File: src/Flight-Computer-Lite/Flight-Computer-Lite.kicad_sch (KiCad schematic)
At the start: 38 parts, among them J1 Jumper_NO, J2 Jumper_NO, P1 1546551-2, P2 3220-20-0200-00, U1 STM32H750VBTx, U2 LMS8117AMP-3.3_NOPB, Y1 ECS-240-18-33-JGN-TR

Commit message: imported footprints into layout
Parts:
- B1: footprint SW_PTS647SM38SMTR2LFS_CNK -> Flight-Computer-Lite:PTS647SM38SMTR2LFS
- C1, C11, C12, C14, C15, C2, C3, C4, C5, C6, C7, C8, C9: footprint Flight-Computer:CAP_0603 -> Flight-Computer-Lite:CAP_0603
- C10, C13: footprint Flight-Computer:T491A106K010AT -> Flight-Computer-Lite:T491A106K010AT
- D1: footprint LED_CLMVC-FKA-CL1D1L71BB7C3C3 -> Flight-Computer-Lite:CLMVC-FKA-CL1D1L71BB7C3C3
- D2, D3: footprint SOD-123FL_MCC -> Flight-Computer-Lite:SM5819PL-TP
- H1, H2, H3: footprint Flight-Computer:MountingHole_3mm -> Flight-Computer-Lite:MountingHole_3mm
- J1, J2: footprint Engine-Controller:Jumper-NO -> Flight-Computer-Lite:Jumper-NO
- LOGO1: footprint Flight-Computer:Logo -> Flight-Computer-Lite:Logo
- P1: footprint Flight-Computer:1546551-2 -> Flight-Computer-Lite:1546551-2
- P2: footprint CONN20_D10-RA-BK_SUL -> Flight-Computer-Lite:3220-20-0200-00
- R1, R2, R3, R4, R5, R6: footprint Flight-Computer:RES_0603 -> Flight-Computer-Lite:RES_0603
- TP1: footprint Flight-Computer:TP -> Flight-Computer-Lite:TP
- U2: footprint Flight-Computer:LMS8117AMP-3.3NOPB -> Flight-Computer-Lite:LMS8117AMP-3.3NOPB
- Y1: footprint Flight-Computer:ECS-240-18-33-JGN-TR -> Flight-Computer-Lite:ECS-240-18-33-JGN-TR

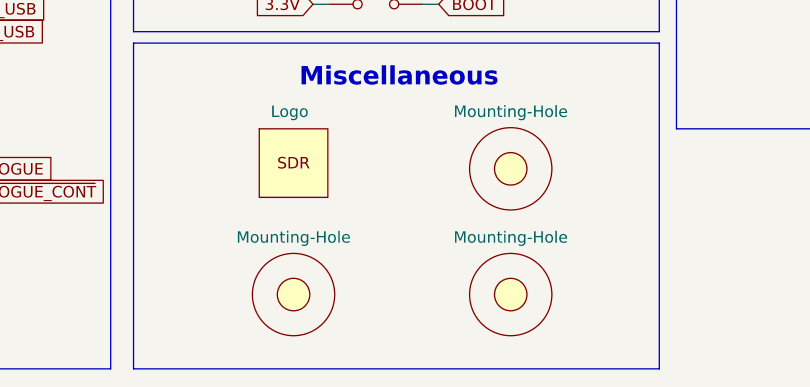
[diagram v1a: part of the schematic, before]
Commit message: finalized board outline and component placements
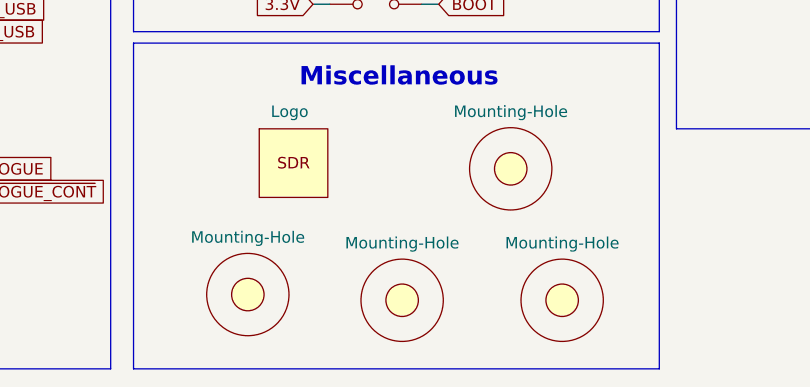
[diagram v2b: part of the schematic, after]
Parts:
- added H4: Mounting-Hole, Flight-Computer-Lite:MountingHole_3mm, symbol Flight-Computer-Lite:Mounting-Hole
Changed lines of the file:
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@@
     (pin "2")
   )
-  (symbol (lib_id "Flight-Computer:Mounting-Hole") (at 135.255 182.88 0) (unit 1)
-    (in_bom yes) (on_board yes)
-    (property "Reference" "H1" (id 0) (at 135.255 176.53 0)
-      (effects (font (size 1.27 1.27)) hide)
-    )
-    (property "Value" "Mounting-Hole" (id 1) (at 135.255 176.53 0))
-    (property "Footprint" "Flight-Computer-Lite:MountingHole_3mm" (id 2) (at 135.255 182.88 0)
-      (effects (font (size 1.27 1.27)) hide)
-    )
-    (property "Datasheet" "" (id 3) (at 135.255 182.88 0)
+  (symbol (lib_id "Flight-Computer:Mounting-Hole") (at 130.175 182.88 0) (unit 1)
+    (in_bom yes) (on_board yes)
+    (property "Reference" "H1" (id 0) (at 130.175 176.53 0)
+      (effects (font (size 1.27 1.27)) hide)
+    )
+    (property "Value" "Mounting-Hole" (id 1) (at 130.175 176.53 0))
+    (property "Footprint" "Flight-Computer-Lite:MountingHole_3mm" (id 2) (at 130.175 182.88 0)
+      (effects (font (size 1.27 1.27)) hide)
+    )
+    (property "Datasheet" "" (id 3) (at 130.175 182.88 0)
       (effects (font (size 1.27 1.27)) hide)
     )
@@
     (pin "3")
   )
-  (symbol (lib_id "Flight-Computer:Mounting-Hole") (at 159.385 182.88 0) (unit 1)
-    (in_bom yes) (on_board yes)
-    (property "Reference" "H3" (id 0) (at 159.385 176.53 0)
-      (effects (font (size 1.27 1.27)) hide)
-    )
-    (property "Value" "Mounting-Hole" (id 1) (at 159.385 176.53 0))
-    (property "Footprint" "Flight-Computer-Lite:MountingHole_3mm" (id 2) (at 159.385 182.88 0)
-      (effects (font (size 1.27 1.27)) hide)
-    )
-    (property "Datasheet" "" (id 3) (at 159.385 182.88 0)
+  (symbol (lib_id "Flight-Computer:Mounting-Hole") (at 165.1 183.515 0) (unit 1)
+    (in_bom yes) (on_board yes)
+    (property "Reference" "H3" (id 0) (at 165.1 177.165 0)
+      (effects (font (size 1.27 1.27)) hide)
+    )
+    (property "Value" "Mounting-Hole" (id 1) (at 165.1 177.165 0))
+    (property "Footprint" "Flight-Computer-Lite:MountingHole_3mm" (id 2) (at 165.1 183.515 0)
+      (effects (font (size 1.27 1.27)) hide)
+    )
+    (property "Datasheet" "" (id 3) (at 165.1 183.515 0)
       (effects (font (size 1.27 1.27)) hide)
     )
@@
     (pin "1")
     (pin "2")
+  )
+  (symbol (lib_id "Flight-Computer-Lite:Mounting-Hole") (at 147.32 183.515 0) (unit 1)
+    (in_bom yes) (on_board yes)
+    (property "Reference" "H4" (id 0) (at 147.32 177.165 0)
+      (effects (font (size 1.27 1.27)) hide)
+    )
+    (property "Value" "Mounting-Hole" (id 1) (at 147.32 177.165 0))
+    (property "Footprint" "Flight-Computer-Lite:MountingHole_3mm" (id 2) (at 147.32 183.515 0)
+      (effects (font (size 1.27 1.27)) hide)
+    )
+    (property "Datasheet" "" (id 3) (at 147.32 183.515 0)
+      (effects (font (size 1.27 1.27)) hide)
+    )
   )
   (symbol (lib_id "Flight-Computer:RES_0603") (at 194.31 117.475 90) (unit 1)
@@
       (reference "H3") (unit 1) (value "Mounting-Hole") (footprint "Flight-Computer-Lite:MountingHole_3mm")
     )
+    (path "/944cc5fc-8368-4f2b-afb2-6569465d7204"
+      (reference "H4") (unit 1) (value "Mounting-Hole") (footprint "Flight-Computer-Lite:MountingHole_3mm")
+    )
     (path "/4676dafd-fe47-412b-a9dc-e9e277c39c39"
       (reference "J1") (unit 1) (value "Jumper_NO") (footprint "Flight-Computer-Lite:Jumper-NO")
@@
     )
     (path "/08e34671-5cef-4537-a872-295f12c49849/0d1be007-740d-43de-9b01-59d1e8f3110e"
-      (reference "U3") (unit 1) (value "SST25VF040B-50-4I-S2AE-T") (footprint "Flight-Computer-Lite:AT-1438-TWT-R")
+      (reference "U3") (unit 1) (value "SST25VF040B-50-4I-S2AE-T") (footprint "Flight-Computer-Lite:SST25VF040B-50-4I-S2AE-T")
     )
     (path "/08e34671-5cef-4537-a872-295f12c49849/12f02691-194e-4d33-a91f-c6007317667b"
@@
     )
     (path "/08e34671-5cef-4537-a872-295f12c49849/1299d8c4-00eb-452c-95bc-607f9b2b516f"
-      (reference "U6") (unit 1) (value "BMP390") (footprint "Flight-Computer-Lite:CAP_0603")
+      (reference "U6") (unit 1) (value "BMP390") (footprint "Flight-Computer-Lite:BMP390")
     )
     (path "/08e34671-5cef-4537-a872-295f12c49849/86cbf718-1c26-4d71-9c40-d417cefe3e2e"

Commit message: finalized rev1 routing
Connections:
- net MAIN: now also U1.5 (PE6); no longer U1.87 (PD6)
- net PROG: now also U1.25 (PA3); no longer U1.45 (PE15)
- net ~{FLASH_HOLD}: now also U1.59 (PD12); no longer U1.60 (PD13)
- net ~{FLASH_WP}: now also U1.60 (PD13); no longer U1.59 (PD12)

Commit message: reduced form factor
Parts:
- B1: footprint Flight-Computer-Lite:PTS647SM38SMTR2LFS -> Flight-Computer:PTS647SM38SMTR2LFS
- LOGO1: footprint Flight-Computer-Lite:Logo -> Flight-Computer-Lite:logo_small
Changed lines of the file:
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@@
       (effects (font (size 1.27 1.27)) (justify left))
     )
-    (property "Footprint" "Flight-Computer-Lite:Logo" (id 2) (at 135.255 168.275 0)
+    (property "Footprint" "Flight-Computer-Lite:logo_small" (id 2) (at 135.255 168.275 0)
       (effects (font (size 1.27 1.27)) hide)
     )
@@
       (effects (font (size 1.524 1.524)) hide)
     )
-    (property "Footprint" "Flight-Computer-Lite:PTS647SM38SMTR2LFS" (id 2) (at 155.575 86.995 0)
+    (property "Footprint" "Flight-Computer:PTS647SM38SMTR2LFS" (id 2) (at 155.575 86.995 0)
       (effects (font (size 1.524 1.524)) hide)
     )
@@
     )
     (path "/3a0eb9ea-d6b2-47ee-9241-4e87debf783d"
-      (reference "B1") (unit 1) (value "PTS647SM38SMTR2LFS") (footprint "Flight-Computer-Lite:PTS647SM38SMTR2LFS")
+      (reference "B1") (unit 1) (value "PTS647SM38SMTR2LFS") (footprint "Flight-Computer:PTS647SM38SMTR2LFS")
     )
     (path "/08e34671-5cef-4537-a872-295f12c49849/d9bd453e-b189-4848-a121-792de11ddfdf"
@@
     )
     (path "/03801c8b-e97e-4a0c-9e94-1165c7d4f44f"
-      (reference "LOGO1") (unit 1) (value "Logo") (footprint "Flight-Computer-Lite:Logo")
+      (reference "LOGO1") (unit 1) (value "Logo") (footprint "Flight-Computer-Lite:logo_small")
     )
     (path "/7c69e08f-34c2-4693-a249-5bdef19868db"

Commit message: created rev2 schematic
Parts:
- removed B1: PTS647SM38SMTR2LFS, Flight-Computer:PTS647SM38SMTR2LFS, symbol Flight-Computer:PTS647SM38SMTR2LFS
- removed C11, C15: 2.2uF, Flight-Computer-Lite:CAP_0603, symbol Flight-Computer:CAP_0603
- removed C3, C5: 0.1uF, Flight-Computer-Lite:CAP_0603, symbol Flight-Computer:CAP_0603
- removed J1: Jumper_NO, Flight-Computer-Lite:Jumper-NO, symbol Flight-Computer:Jumper_NO
- removed P2: 3220-20-0200-00, Flight-Computer-Lite:3220-20-0200-00, symbol Flight-Computer:3220-20-0200-00
- removed TP1: TP, Flight-Computer-Lite:TP, symbol Flight-Computer:TP
- removed U1: STM32H750VBTx, Flight-Computer-Lite:STM32H750VBT6, symbol Flight-Computer-Lite:STM32H750VBTx
- added C8, C9: 0.1uF, Flight-Computer-Lite:CAP_0603, symbol Flight-Computer:CAP_0603
- added P1: 1984659, Flight-Computer-Lite:1984659, symbol Flight-Computer:1984659
- added P2: USB, Flight-Computer-Lite:10118194-0001LF, symbol Flight-Computer-Lite:USB
- added P3: 0530470610, Flight-Computer-Lite:53047-0610, symbol Flight-Computer-Lite:0530470610
- added Q1, Q4: QS5U17TR, Flight-Computer-Lite:QS5U17TR, symbol Flight-Computer:QS5U17TR
- added Q2, Q3: 2N7002W-7-F, Flight-Computer-Lite:2N7002W-7-F, symbol Flight-Computer-Lite:2N7002W-7-F
- added R1, R3, R7, R8, R9: 10k, Flight-Computer-Lite:RES_0603, symbol Flight-Computer:RES_0603
- added R10, R2: 100k, Flight-Computer-Lite:RES_0603, symbol Flight-Computer:RES_0603
- added R11: 20k, Flight-Computer-Lite:RES_0603, symbol Flight-Computer:RES_0603
- added R12, R13: 4.7k, Flight-Computer-Lite:RES_0603, symbol Flight-Computer:RES_0603
- added U1: STM32G4A1KEU6, Flight-Computer-Lite:STM32G4A1KEU6, symbol Flight-Computer-Lite:STM32G4A1KEU6
- added U2: BMP390, Flight-Computer-Lite:BMP390, symbol Flight-Computer:BMP390
- C4: renamed from C8; value 0.1uF -> 0.01uF
- C6, C7: value 0.1uF -> 1uF
- renumbered C2 to C1, C12 to C10, C14 to C11, C10 to C12, C4 to C2, C1 to C3, C9 to C5, D4 to D3, D3 to D4, H2 to H1, H1 to H2, H4 to H3, H3 to H4, J2 to J1, P1 to P4, R4 to R14, R5 to R15, R6 to R16, R1 to R4, R2 to R5, R3 to R6, U2 to U3
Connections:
- net 3.3V: now also C8.1, C9.1, P3.1, R1.2, R12.2, R13.2, R7.2, U1.1 (VDD), U1.15 (VDDA), U1.17 (VDD), U2.1 (VDDIO), U2.10 (VDD), U2.6 (CSB); no longer C6.1, C7.1
- net 5V: now also P2.1 (VCC), R8.2
- net BEEP: now also U1.7 (PA2)
- net BOOT: now also U1.31 (PB8-BOOT0)
- net BP_SCL: now also R12.1, U1.19 (PA9), U2.2 (SCK)
- net BP_SDA: now also R13.1, U1.18 (PA8), U2.4 (SDI)
- net DROGUE: now also C7.1, Q4.1 (G), R10.2, U1.27 (PB4)
- net Earth: now also C8.2, C9.2, P2.5 (GND), P2.S1 (SHIELD), P2.S2 (SHIELD), P3.6, Q1.2 (S), Q2.2 (S), Q3.2 (S), Q4.2 (S), R10.1, R11.1, R2.1, R3.1, R9.1, U1.14 (VSSA), U1.16 (VSS), U1.32 (VSS), U2.3 (VSS), U2.5 (SDO), U2.8 (VSS), U2.9 (VSS)
- net FLASH_MISO: now also U1.13 (PB0)
- net FLASH_MOSI: now also U1.12 (PA7)
- net FLASH_SCK: now also U1.10 (PA5)
- net MAIN: now also C6.1, Q1.1 (G), R2.2, U1.8 (PA3)
- net NRST: now also P3.5, U1.4 (PG10-NRST)
- net OSC_IN: now also U1.2 (PF0-OSC_IN)
- net OSC_OUT: now also U1.3 (PF1-OSC_OUT)
- net PROG: now also U1.20 (PA10)
- net STATUS_B: now also U1.30 (PB7)
- net STATUS_G: now also U1.29 (PB6)
- net STATUS_R: now also U1.28 (PB5)
- net SWCLK: now also P3.3, U1.24 (PA14)
- net SWDIO: now also P3.2, U1.23 (PA13)
- net SWO: now also P3.4, U1.26 (PB3)
- net USB_DETECT: now also R11.2, R8.1, U1.5 (PA0)
- net ~{DROGUE_CONT}: now also Q3.3 (D), R7.1, U1.25 (PA15)
- net ~{FLASH_SS}: now also U1.11 (PA6)
- net ~{MAIN_CONT}: now also Q2.3 (D), R1.1, U1.9 (PA4)
- net ~{SWITCH}: now also U1.6 (PA1)
- net PIN_SCREW: no longer names the net of D4.2, P4.1 (5)
- new net: P1.4 (6), Q1.5 (D), Q2.1 (G), R3.2
- new net: P1.6, Q3.1 (G), Q4.5 (D), R9.2
- new net USB_D+: P2.3 (D+), U1.22 (PA12)
- new net USB_D-: P2.2 (D-), U1.21 (PA11)
- new net VIN_SW: P1.3 (5), P1.5
- no-connect marks 59 -> 3
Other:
- removed sheet Peripherals
- added sheet Sheet2 (Sheet2.kicad_sch)
- note added: "Barometric Pressure Sensor and Temperature Sensor"
- note added: "Drogue Chute Deployment"
- note added: "Main Chute Deployment"
- note added: "Power Detector"
- note added: "USB"
- note removed: "MCU Internal Regulator Caps"
- note removed: "MCU Reset"
- moved on the sheet: C1, C10, C11, C12, C13, C2, C3, C4, C5, D1, D2, D3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
